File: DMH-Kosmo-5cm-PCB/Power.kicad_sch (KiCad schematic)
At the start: 13 parts, among them J100 IDC_02x08, J101 IDC_02x05

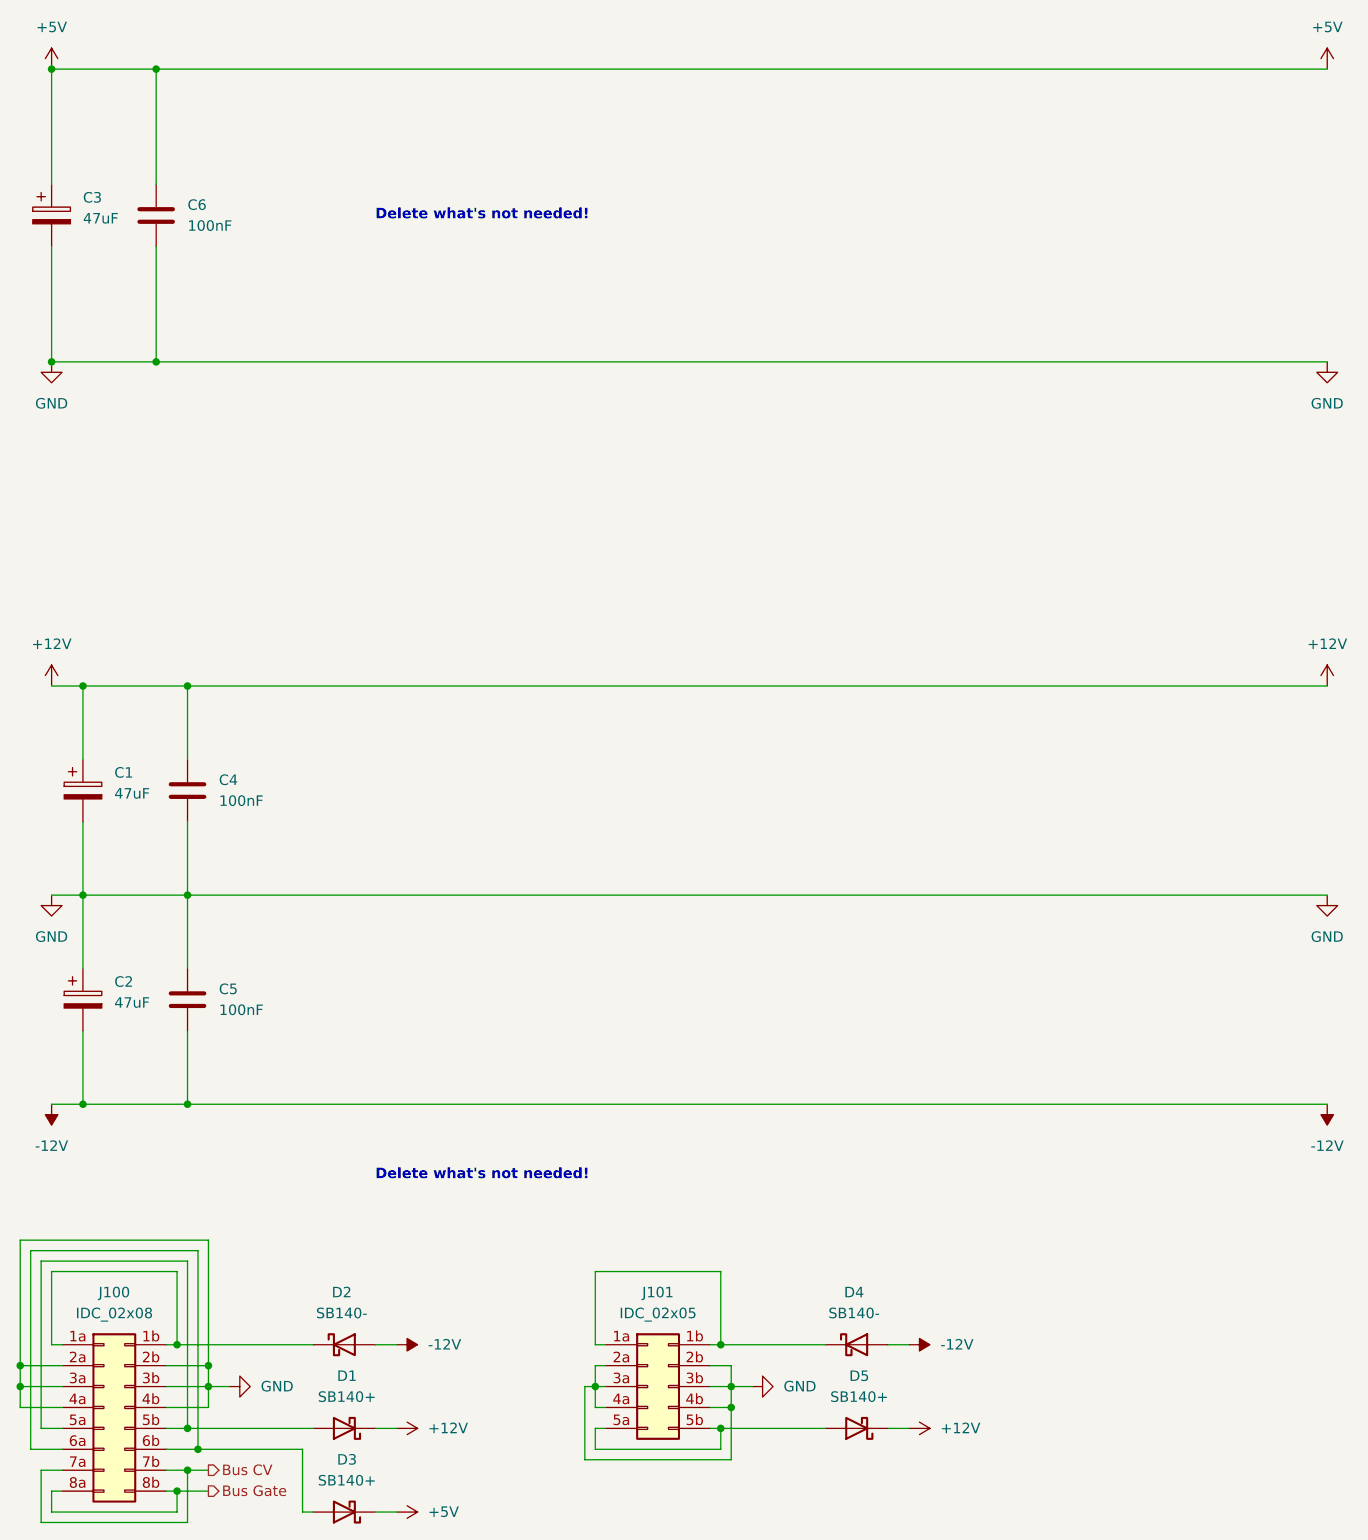
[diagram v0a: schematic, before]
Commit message: Created 5cm PCB template
And updated power sheet of 10cm template
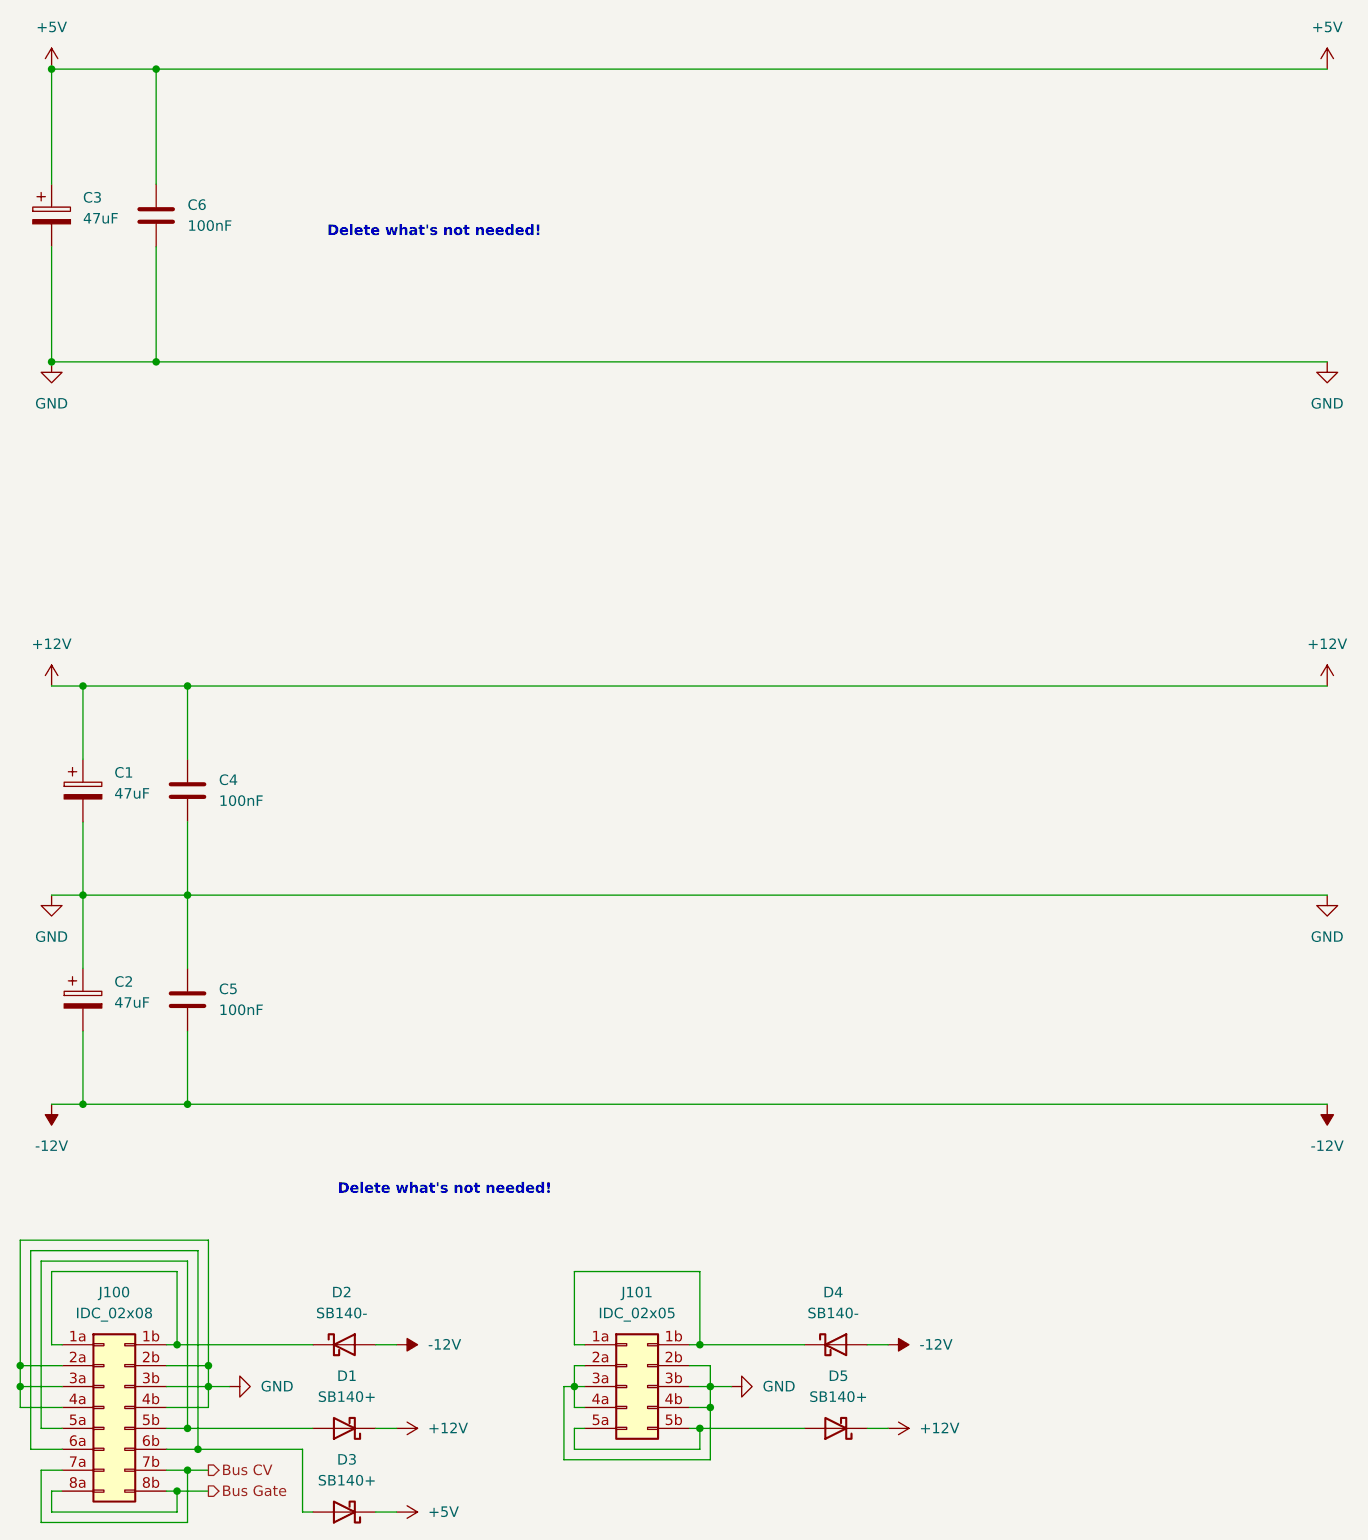
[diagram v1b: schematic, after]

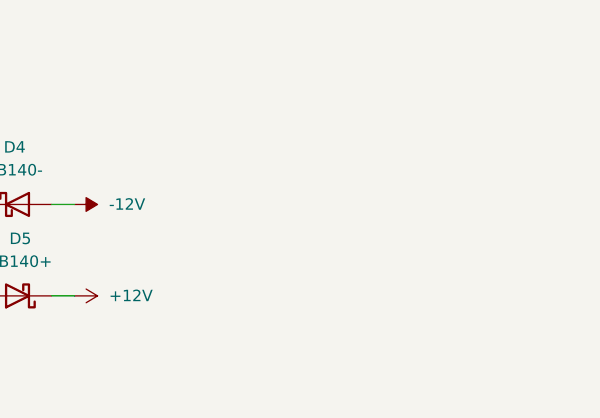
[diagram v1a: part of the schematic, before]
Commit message: Updated 5cm and 10 templates
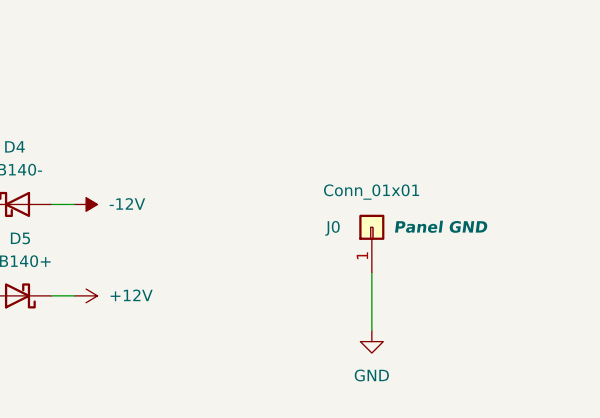
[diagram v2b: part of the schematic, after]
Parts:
- added J0: Conn_01x01, Connector_PinHeader_2.54mm:PinHeader_1x01_P2.54mm_Vertical, symbol Connector_Generic:Conn_01x01
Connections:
- net GND: now also J0.1 (Pin_1)
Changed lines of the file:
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@@
+	(wire
+		(pts
+			(xy 152.4 182.88) (xy 152.4 189.23)
+		)
+		(stroke
+			(width 0)
+			(type default)
+		)
+	)
 	(wire
 		(pts
@@
 	)
 	(symbol
+		(lib_id "Connector_Generic:Conn_01x01")
+		(at 152.4 177.8 90)
+		(unit 1)
+		(exclude_from_sim no)
+		(in_bom yes)
+		(on_board yes)
+		(dnp no)
+		(property "Reference" "J0"
+			(at 147.32 177.8 90)
+			(effects
+				(font
+					(size 1.27 1.27)
+				)
+				(justify right)
+			)
+		)
+		(property "Value" "Conn_01x01"
+			(at 152.4 173.736 90)
+			(effects
+				(font
+					(size 1.27 1.27)
+				)
+			)
+		)
+		(property "Footprint" "Connector_PinHeader_2.54mm:PinHeader_1x01_P2.54mm_Vertical"
+			(at 152.4 177.8 0)
+			(effects
+				(font
+					(size 1.27 1.27)
+				)
+				(hide yes)
+			)
+		)
+		(property "Datasheet" "~"
+			(at 152.4 177.8 0)
+			(effects
+				(font
+					(size 1.27 1.27)
+				)
+				(hide yes)
+			)
+		)
+		(property "Description" "Generic connector, single row, 01x01, script generated (kicad-library-utils/schlib/autogen/connector/)"
+			(at 152.4 177.8 0)
+			(effects
+				(font
+					(size 1.27 1.27)
+				)
+				(hide yes)
+			)
+		)
+		(property "Function" "Panel GND"
+			(at 160.02 177.8 90)
+			(effects
+				(font
+					(size 1.27 1.27)
+					(thickness 0.254)
+					(bold yes)
+					(italic yes)
+				)
+			)
+		)
+		(pin "1"
+		)
+		(instances
+			(project "DMH-Kosmo-5cm-PCB"
+				(path "/58f4306d-5387-4983-bb08-41a2313fd315/0cdf34b2-39cd-4d9e-981a-97cd34791509"
+					(reference "J0")
+					(unit 1)
+				)
+			)
+		)
+	)
+	(symbol
 		(lib_id "power:+12V")
 		(at 17.78 95.25 0)
@@
 	)
 	(symbol
+		(lib_id "power:GND")
+		(at 152.4 189.23 0)
+		(unit 1)
+		(exclude_from_sim no)
+		(in_bom yes)
+		(on_board yes)
+		(dnp no)
+		(fields_autoplaced yes)
+		(property "Reference" "#PWR08"
+			(at 152.4 195.58 0)
+			(effects
+				(font
+					(size 1.27 1.27)
+				)
+				(hide yes)
+			)
+		)
+		(property "Value" "GND"
+			(at 152.4 194.31 0)
+			(effects
+				(font
+					(size 1.27 1.27)
+				)
+			)
+		)
+		(property "Footprint" ""
+			(at 152.4 189.23 0)
+			(effects
+				(font
+					(size 1.27 1.27)
+				)
+				(hide yes)
+			)
+		)
+		(property "Datasheet" ""
+			(at 152.4 189.23 0)
+			(effects
+				(font
+					(size 1.27 1.27)
+				)
+				(hide yes)
+			)
+		)
+		(property "Description" "Power symbol creates a global label with name \"GND\" , ground"
+			(at 152.4 189.23 0)
+			(effects
+				(font
+					(size 1.27 1.27)
+				)
+				(hide yes)
+			)
+		)
+		(pin "1"
+		)
+		(instances
+			(project "DMH-Kosmo-5cm-PCB"
+				(path "/58f4306d-5387-4983-bb08-41a2313fd315/0cdf34b2-39cd-4d9e-981a-97cd34791509"
+					(reference "#PWR08")
+					(unit 1)
+				)
+			)
+		)
+	)
+	(symbol
 		(lib_id "power:+5V")
 		(at 59.69 195.58 270)
@@
 			)
 		)
+		(property "Function" ""
+			(at 24.13 182.88 0)
+			(effects
+				(font
+					(size 1.27 1.27)
+				)
+			)
+		)

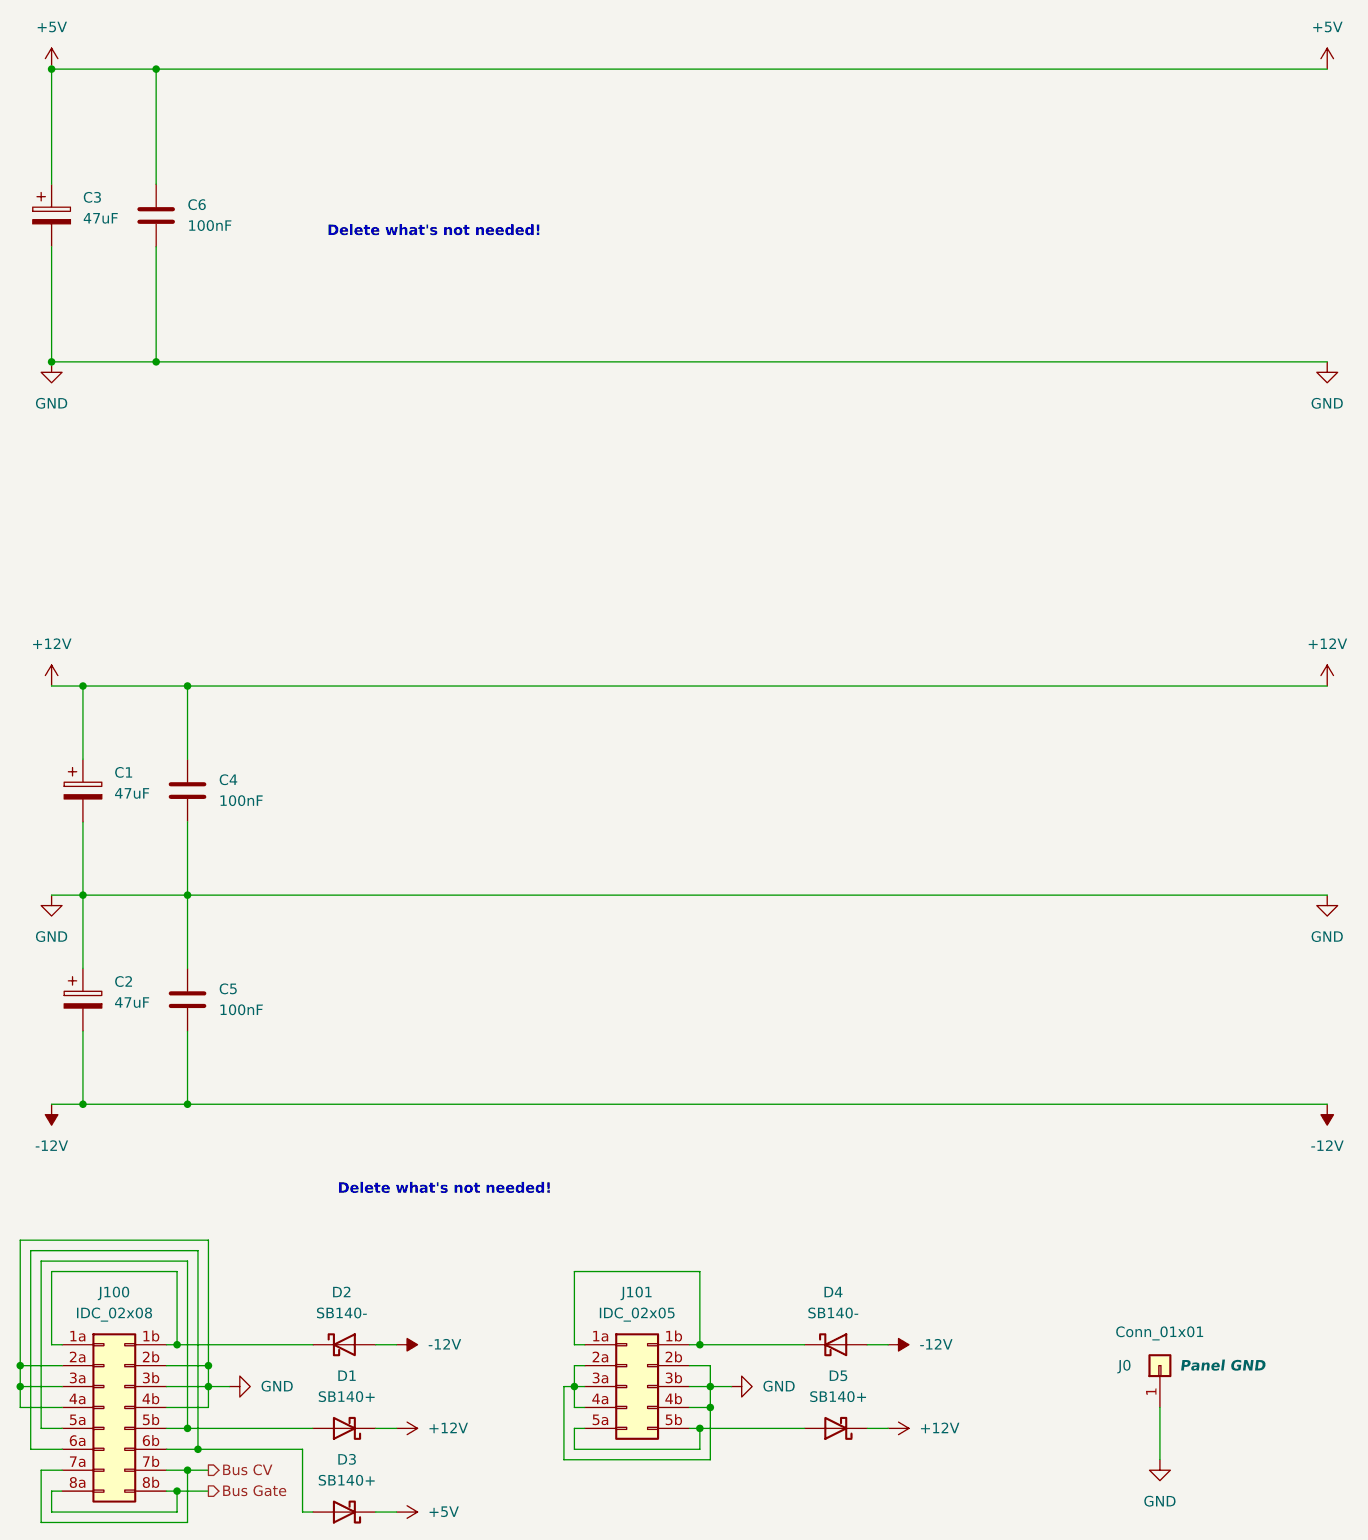
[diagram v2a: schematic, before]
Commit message: Minor fixes on schematic templates
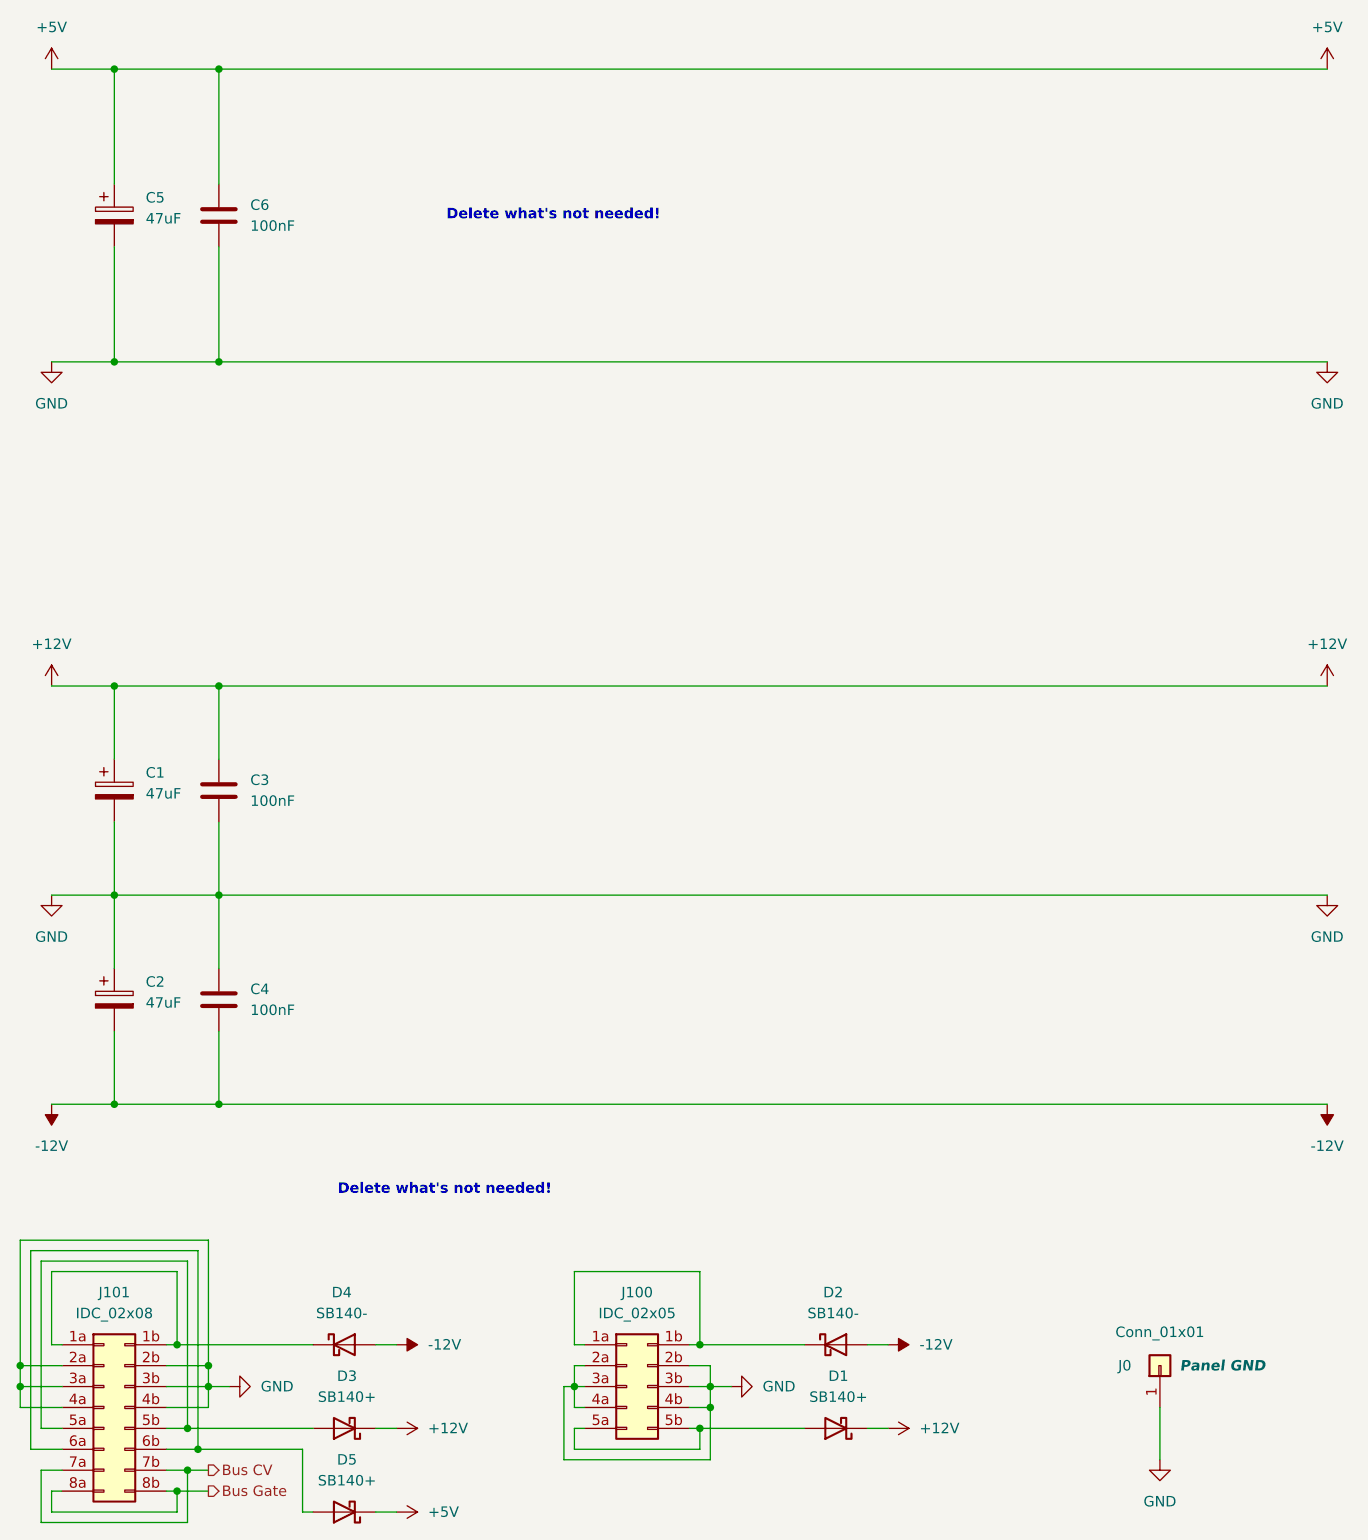
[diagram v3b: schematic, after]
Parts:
- renumbered C4 to C3, C5 to C4, C3 to C5, D5 to D1, D4 to D2, D1 to D3, D2 to D4, D3 to D5, J101 to J100, J100 to J101
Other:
- moved on the sheet: C1, C2, C3, C4, C5, C6
